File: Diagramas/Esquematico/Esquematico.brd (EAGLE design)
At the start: 63.3 x 80.1 mm, 48 parts, among them IC3 DS3231N_DIP, IC4 3071_SMD, J1 Modulo Pir, J2 RASPBERRYPI-40-PIN-GPIO_SMT, K1 SRD-05VDC-SL-C, K2 SRD-05VDC-SL-C, K3 SRD-05VDC-SL-C, K4 SRD-05VDC-SL-C, U1 RFM69HW-868S2

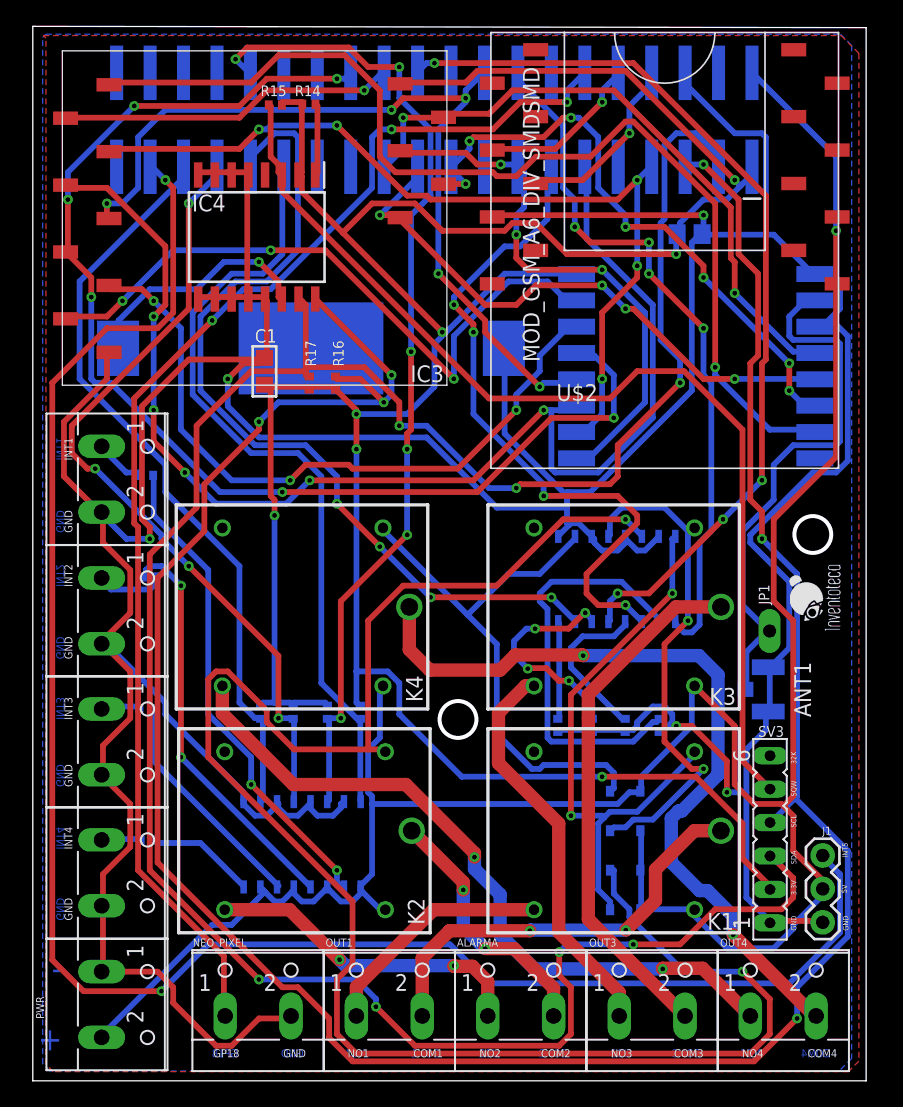
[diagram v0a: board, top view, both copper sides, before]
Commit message: Pcb con Smd
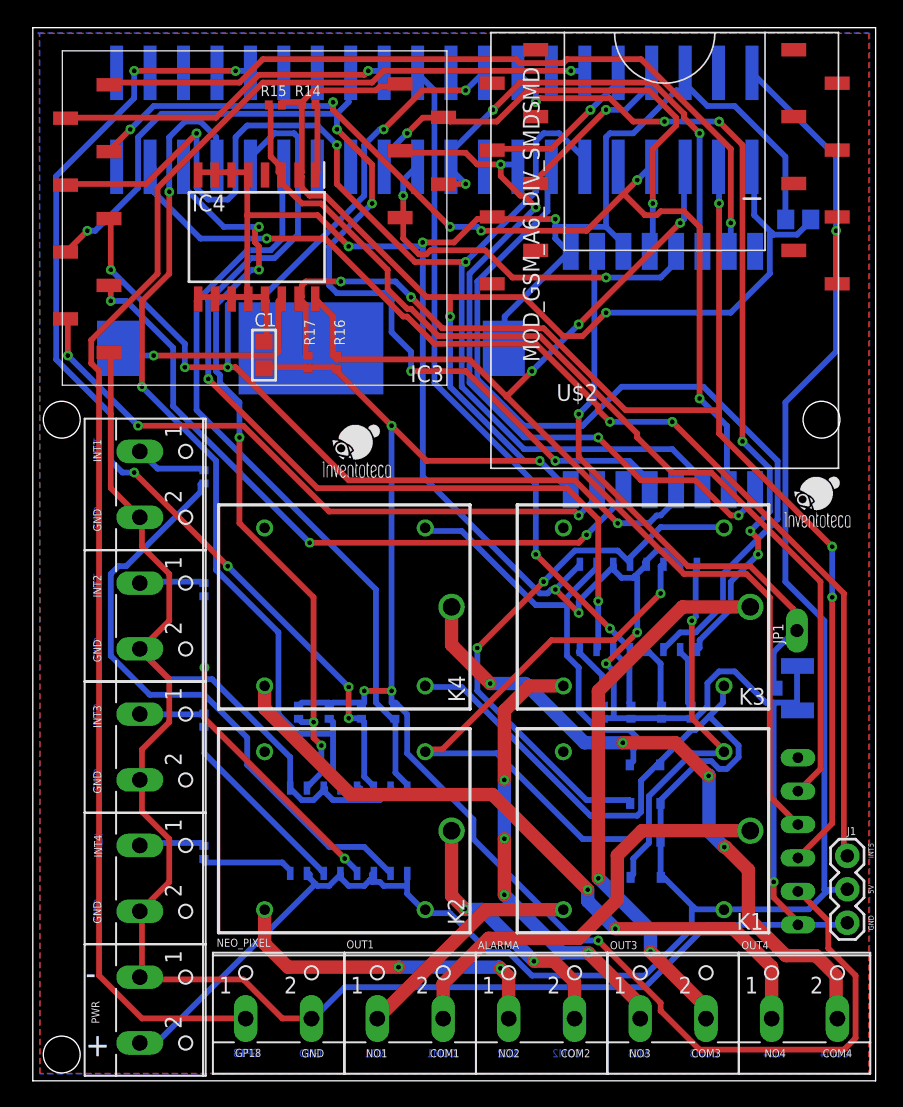
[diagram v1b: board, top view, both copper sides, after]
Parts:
- moved C3 8.33 mm to (58.1, 65.4), turned to 0 degrees
- moved R8 4.48 mm to (13.0, 27.4), turned to 90 degrees
- moved R9 4.40 mm to (13.0, 17.4), turned to 90 degrees
- moved R6 4.36 mm to (13.0, 45.9), turned to 270 degrees
- moved R7 4.23 mm to (13.0, 37.3), turned to 270 degrees
- moved OK1 3.69 mm to (24.0, 19.0)
- moved R4 3.59 mm to (43.3, 28.0)
- moved K4 3.21 mm to (31.8, 36.0)
- moved R3 3.11 mm to (45.4, 28.0)
- moved K2 3.03 mm to (31.8, 19.0)
- moved R2 2.94 mm to (47.8, 28.0)
- moved INT4 2.93 mm to (9.40, 15.4)
- moved PWR 2.93 mm to (9.40, 5.38)
- moved INT1 2.93 mm to (9.40, 45.3)
- moved INT2 2.93 mm to (9.40, 35.3)
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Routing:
- net SCL: track 194.5 -> 87.0 mm, vias 6 -> 3
- net N$34: track 137.4 -> 43.7 mm, vias 2 -> 1
- net SDA: track 182.6 -> 98.9 mm, vias 7 -> 5
- net INT5: track 138.6 -> 87.4 mm, vias 2 -> 3
- net GND: track 368.3 -> 339.7 mm, vias 5 -> 8
- net N$10: track 31.5 -> 4.61 mm
- net G2: track 65.6 -> 91.3 mm, vias 5 -> 6
- net CS: track 80.4 -> 59.0 mm
- net OUT3: track 69.7 -> 50.5 mm, vias 4 -> 2
- net MISO: track 44.5 -> 29.7 mm, vias 4 -> 2
- net N$35: track 43.8 -> 29.2 mm, vias 2 -> 1
- net RST_LORA: track 42.1 -> 56.5 mm, vias 3 -> 4
- net G3: track 93.6 -> 79.6 mm, vias 6 -> 5
- net G18: track 97.0 -> 110.8 mm, vias 3 -> 1
- net OUT_ALARMA: track 52.0 -> 65.0 mm, vias 4 -> 0
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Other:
- board size 63.3 x 80.1 mm -> 64 x 80 mm

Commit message: Pcb "Terminado"
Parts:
- moved ANT1 30.6 mm to (33.6, 48.2), flipped to the top, turned to 270 degrees
- moved J1 26.0 mm to (58.0, 37.7)
- moved SV3 1.03 mm to (58.9, 18.9), flipped to the top
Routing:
- net INT5: track 87.4 -> 133.9 mm, vias 3 -> 4
- net N$32: track 33.3 -> 67.8 mm, vias 0 -> 1
- net GND: track 339.7 -> 373.7 mm, vias 8 -> 5
- net 5V: track 195.8 -> 163.1 mm, vias 1 -> 2
- net 3.3V: track 206.8 -> 238.9 mm, vias 7 -> 6
- net ANT_LORA: track 44.3 -> 71.1 mm, vias 1 -> 7
- net G18: track 110.8 -> 137.2 mm
- net OUT_ALARMA: track 65.0 -> 41.3 mm, vias 0 -> 2
- net N$34: track 43.7 -> 62.2 mm
- net G0: track 77.2 -> 94.3 mm, vias 6 -> 5
- net INT2: track 76.8 -> 61.3 mm, vias 6 -> 0
- net SDA: track 98.9 -> 112.7 mm, vias 5 -> 4
- net G1: track 95.7 -> 83.3 mm, vias 3 -> 4
- net G3: track 79.6 -> 90.7 mm, vias 5 -> 8
- net N$4: track 45.8 -> 35.5 mm, vias 0 -> 2
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
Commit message: Cambio de lugar
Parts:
- removed BT2: BU2032SM-BT-GTR, BU2032SM-BT-GTR:BAT_BU2032SM-BT-GTR
- removed SV3: (no value), con-lsta:FE06
- added B1: (no value), microbuilder:CR1220
- added J3: (no value), SparkFun-Connectors:1X05
- moved ANT1 25.9 mm to (58.5, 55.2)
- moved J1 2.88 mm to (60.9, 37.7)
- moved JP1 2.87 mm to (60.9, 34.2)
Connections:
- removed net 32K: SV3.6
- new net NC: J3.2
- net 3.3V: now also J3.5; no longer SV3.2
- net GND: now also B1.-, J3.1; no longer BT2.2, SV3.1
- net SCL: now also J3.3; no longer SV3.4
- net SDA: now also J3.4; no longer SV3.3
- net SQW: no longer SV3.5
- net VBAT: now also B1.+$1; no longer BT2.1
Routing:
- net SQW: track 81.3 -> 5.77 mm
- net INT2: track 61.3 -> 129.4 mm, vias 0 -> 4
- net INT5: track 133.9 -> 67.4 mm, vias 4 -> 5
- net SCL: track 95.2 -> 138.5 mm, vias 7 -> 5
- net GND: track 373.7 -> 337.6 mm, vias 5 -> 4
- net 3.3V: track 238.9 -> 203.4 mm, vias 6 -> 7
- net ANT_LORA: track 71.1 -> 42.2 mm, vias 7 -> 2
- net N$32: track 67.8 -> 40.2 mm
- net 5V: track 163.1 -> 188.8 mm
- net G18: track 137.2 -> 115.9 mm, vias 1 -> 5
- net COM3: track 51.7 -> 36.0 mm, vias 1 -> 2
- net INT4: track 59.6 -> 73.1 mm, vias 2 -> 3
- net OUT4: track 63.1 -> 73.0 mm, vias 2 -> 6
- net G4: track 55.2 -> 45.9 mm, vias 5 -> 3
- net MOSI: track 32.8 -> 24.1 mm, vias 3 -> 2
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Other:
- board text added: "nc"
- board text removed: "32K"
- board text removed: "SQW"
